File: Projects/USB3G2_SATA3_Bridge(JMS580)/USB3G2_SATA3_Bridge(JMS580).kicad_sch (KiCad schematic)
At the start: 74 parts, among them J1 ATA-A, J2 USB_C_Receptacle, Q1 Q_NPN_EBC, Q2 AO3401A, Q3 AO3400A, U1 W25Q32JVZP, U2 JMS580, U3 FP6381A, Y1 Crystal_GND24

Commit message: finish prj USB3G2_SATA3_Bridge(JMS580)
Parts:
- added H4: MountingHole, Symbol:ESD-Logo_6.6x6mm_SilkScreen, symbol Mechanical:MountingHole
- R1: footprint Resistor_SMD:R_0402_1005Metric -> Resistor_SMD:R_0603_1608Metric
- TP1, TP2: footprint (none) -> TestPoint:TestPoint_Pad_D1.0mm
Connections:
- no-connect marks 7 -> 9
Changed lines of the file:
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@@
   (no_connect (at 39.37 63.5))
   (no_connect (at 39.37 58.42))
+  (no_connect (at 133.35 115.57))
+  (no_connect (at 133.35 113.03))
   (no_connect (at 134.62 115.57))
   (no_connect (at 134.62 113.03))
@@
       (effects (font (size 1.27 1.27)) (justify left) hide)
     )
-    (property "Footprint" "" (id 2) (at 172.72 185.42 0)
+    (property "Footprint" "TestPoint:TestPoint_Pad_D1.0mm" (id 2) (at 172.72 185.42 0)
       (effects (font (size 1.27 1.27)) hide)
     )
@@
       (effects (font (size 1.27 1.27)) (justify left) hide)
     )
-    (property "Footprint" "" (id 2) (at 172.72 187.96 0)
+    (property "Footprint" "TestPoint:TestPoint_Pad_D1.0mm" (id 2) (at 172.72 187.96 0)
       (effects (font (size 1.27 1.27)) hide)
     )
@@
     )
   )
+  (symbol (lib_id "Mechanical:MountingHole") (at 44.45 213.36 0) (unit 1)
+    (in_bom yes) (on_board yes) (fields_autoplaced)
+    (property "Reference" "H4" (id 0) (at 46.99 212.4515 0)
+      (effects (font (size 1.27 1.27)) (justify left))
+    )
+    (property "Value" "MountingHole" (id 1) (at 46.99 215.2266 0)
+      (effects (font (size 1.27 1.27)) (justify left))
+    )
+    (property "Footprint" "Symbol:ESD-Logo_6.6x6mm_SilkScreen" (id 2) (at 44.45 213.36 0)
+      (effects (font (size 1.27 1.27)) hide)
+    )
+    (property "Datasheet" "~" (id 3) (at 44.45 213.36 0)
+      (effects (font (size 1.27 1.27)) hide)
+    )
+  )
   (symbol (lib_id "power:GND") (at 229.87 52.07 0) (unit 1)
     (in_bom yes) (on_board yes)
@@
     (property "Reference" "R1" (id 0) (at 251.46 154.94 90))
     (property "Value" "0R" (id 1) (at 251.46 152.4 90))
-    (property "Footprint" "Resistor_SMD:R_0402_1005Metric" (id 2) (at 251.46 153.162 90)
+    (property "Footprint" "Resistor_SMD:R_0603_1608Metric" (id 2) (at 251.46 153.162 90)
       (effects (font (size 1.27 1.27)) hide)
     )
@@
       (reference "H3") (unit 1) (value "MountingHole") (footprint "MountingHole:MountingHole_2.2mm_M2_Pad_Via")
     )
+    (path "/aa5e381f-9af5-4fa9-8bc8-1fe45b001137"
+      (reference "H4") (unit 1) (value "MountingHole") (footprint "Symbol:ESD-Logo_6.6x6mm_SilkScreen")
+    )
     (path "/b97d5994-9bcb-4763-85c8-744d5971f71d"
       (reference "J1") (unit 1) (value "ATA-A") (footprint "lib:SATA-22P-M")
@@
     )
     (path "/f19ab928-a71b-4fdd-893d-289cb4b88ac7"
-      (reference "R1") (unit 1) (value "0R") (footprint "Resistor_SMD:R_0402_1005Metric")
+      (reference "R1") (unit 1) (value "0R") (footprint "Resistor_SMD:R_0603_1608Metric")
     )
     (path "/25f163c8-b901-4e86-8aef-3e24ed3f1f2b"
@@
     )
     (path "/9324a5d8-df10-40f4-a586-be13060eaaaa"
-      (reference "TP1") (unit 1) (value "TestPoint") (footprint "")
+      (reference "TP1") (unit 1) (value "TestPoint") (footprint "TestPoint:TestPoint_Pad_D1.0mm")
     )
     (path "/96bcae62-54a4-4017-ba90-ec5c8ae58df7"
-      (reference "TP2") (unit 1) (value "TestPoint") (footprint "")
+      (reference "TP2") (unit 1) (value "TestPoint") (footprint "TestPoint:TestPoint_Pad_D1.0mm")
     )
     (path "/3f90ca07-e4d3-4f1b-91dd-571765506dae"

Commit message: add new prj
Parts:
- Q1: footprint Package_TO_SOT_SMD:TSOT-23 -> Package_TO_SOT_SMD:SOT-23
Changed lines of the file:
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@@
       (effects (font (size 1.27 1.27)) (justify left))
     )
-    (property "Footprint" "Package_TO_SOT_SMD:TSOT-23" (id 2) (at 251.46 119.38 0)
+    (property "Footprint" "Package_TO_SOT_SMD:SOT-23" (id 2) (at 251.46 119.38 0)
       (effects (font (size 1.27 1.27)) hide)
     )
@@
     )
     (path "/1edb2be0-b3e0-46f5-bfe4-e9c67541b25b"
-      (reference "Q1") (unit 1) (value "Q_NPN_EBC") (footprint "Package_TO_SOT_SMD:TSOT-23")
+      (reference "Q1") (unit 1) (value "Q_NPN_EBC") (footprint "Package_TO_SOT_SMD:SOT-23")
     )
     (path "/4d95e323-6704-4eb1-a19c-f033972fd2a0"

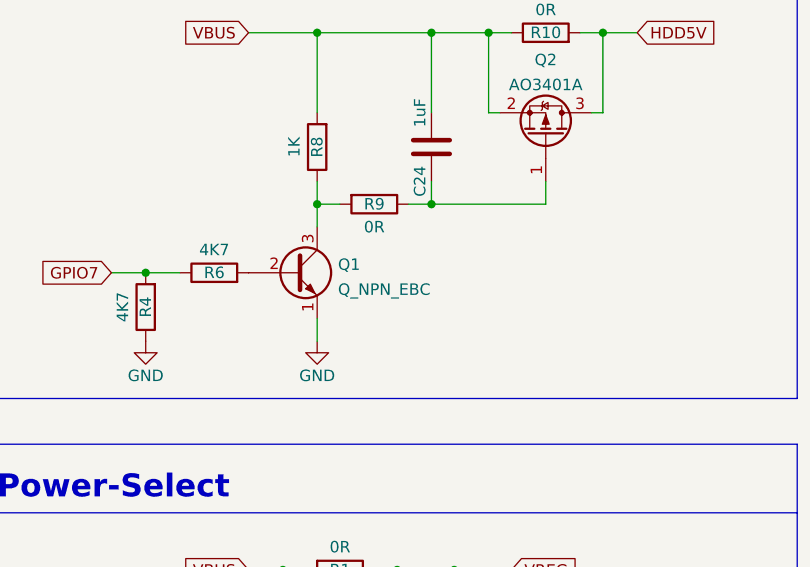
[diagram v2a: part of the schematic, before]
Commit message: Fix USB3G2_SATA3_Bridge(JMS580) 1AM Pinout
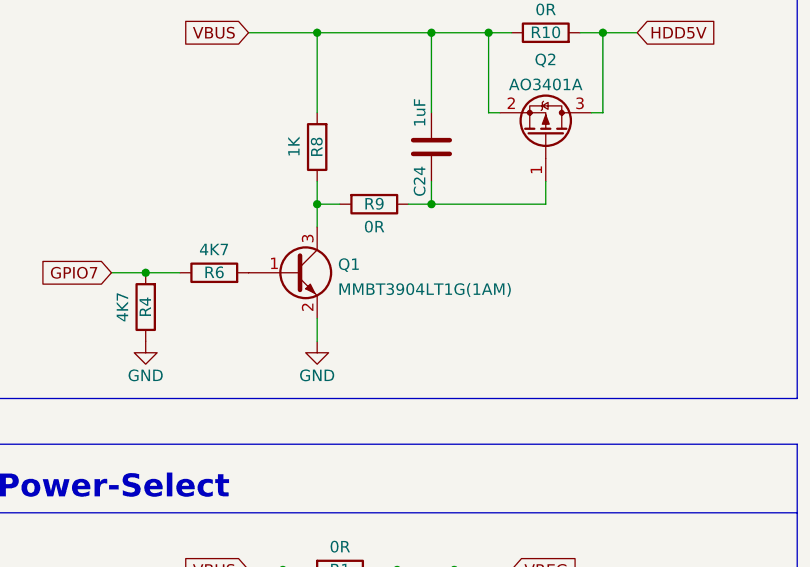
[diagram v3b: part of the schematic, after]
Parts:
- Q1: value Q_NPN_EBC -> MMBT3904LT1G(1AM); symbol Device:Q_NPN_EBC -> Device:Q_NPN_BEC
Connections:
- net GND: now also Q1.2 (E); no longer Q1.1 (E)
- net at R6.2: now also Q1.1 (B); no longer Q1.2 (B)
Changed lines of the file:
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@@
     (pin "2")
   )
-  (symbol (lib_id "Device:Q_NPN_EBC") (at 246.38 121.92 0) (unit 1)
+  (symbol (lib_id "Device:Q_NPN_BEC") (at 246.38 121.92 0) (unit 1)
     (in_bom yes) (on_board yes) (fields_autoplaced)
     (property "Reference" "Q1" (id 0) (at 251.2314 121.0115 0)
       (effects (font (size 1.27 1.27)) (justify left))
     )
-    (property "Value" "Q_NPN_EBC" (id 1) (at 251.2314 123.7866 0)
+    (property "Value" "MMBT3904LT1G(1AM)" (id 1) (at 251.2314 123.7866 0)
       (effects (font (size 1.27 1.27)) (justify left))
     )
@@
     )
     (path "/1edb2be0-b3e0-46f5-bfe4-e9c67541b25b"
-      (reference "Q1") (unit 1) (value "Q_NPN_EBC") (footprint "Package_TO_SOT_SMD:SOT-23")
+      (reference "Q1") (unit 1) (value "MMBT3904LT1G(1AM)") (footprint "Package_TO_SOT_SMD:SOT-23")
     )
     (path "/4d95e323-6704-4eb1-a19c-f033972fd2a0"

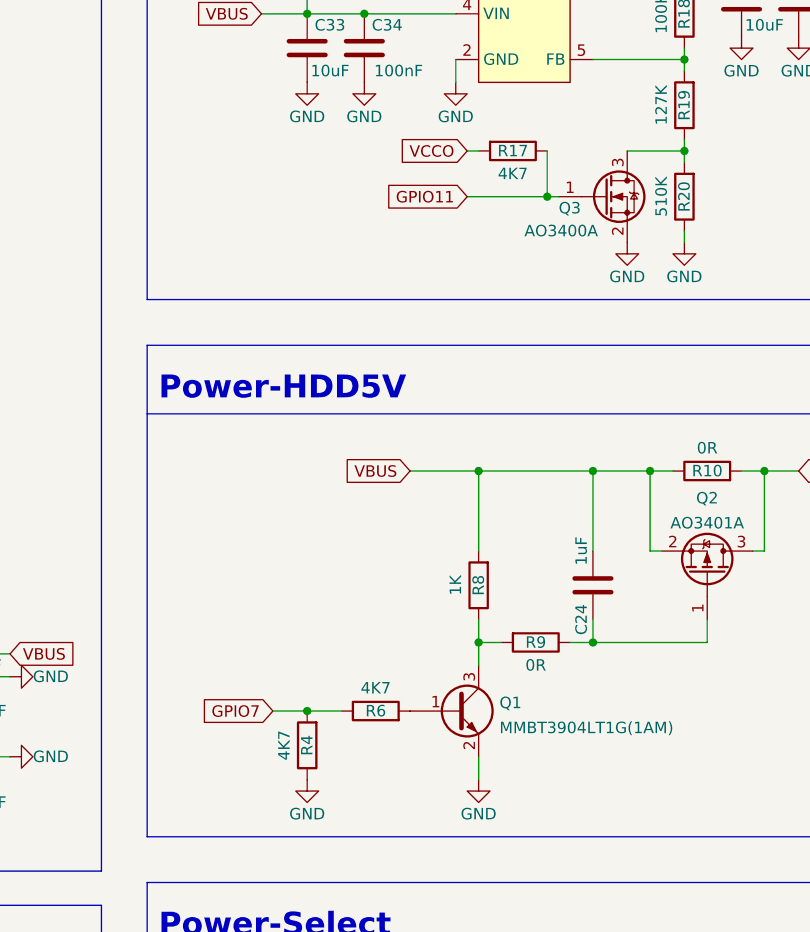
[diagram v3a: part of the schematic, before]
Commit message: Symbol Value unified
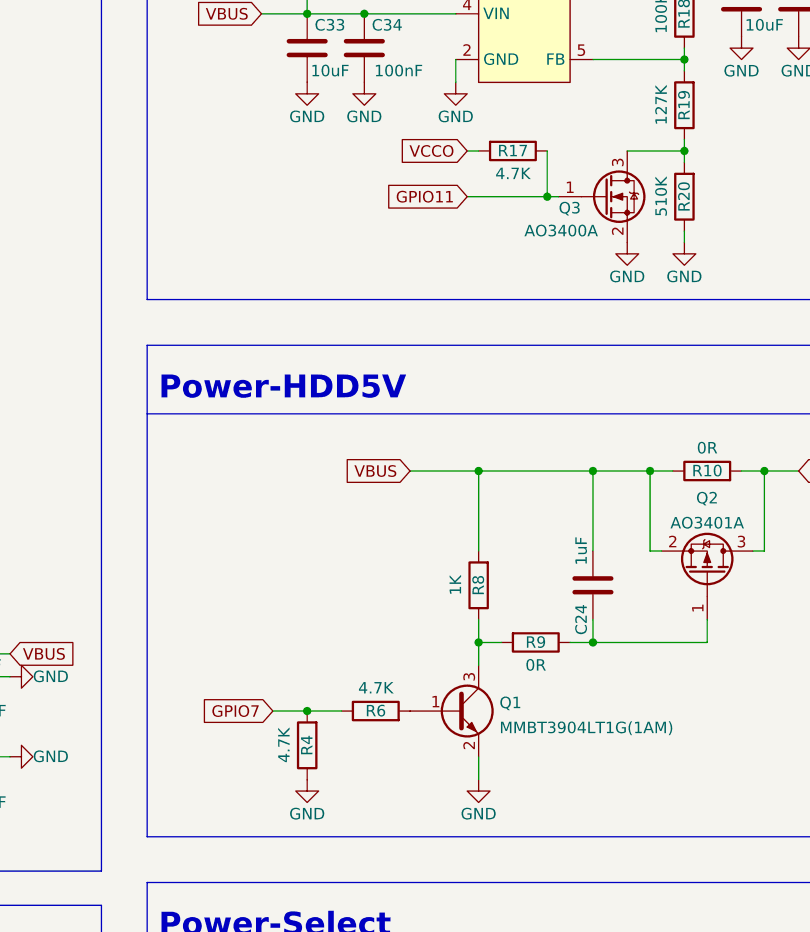
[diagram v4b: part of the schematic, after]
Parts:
- R17, R4, R6: value 4K7 -> 4.7K
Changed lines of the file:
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@@
     (in_bom yes) (on_board yes)
     (property "Reference" "R4" (id 0) (at 229.87 125.73 90))
-    (property "Value" "4K7" (id 1) (at 227.33 125.73 90))
+    (property "Value" "4.7K" (id 1) (at 227.33 125.73 90))
     (property "Footprint" "Resistor_SMD:R_0402_1005Metric" (id 2) (at 231.648 125.73 90)
       (effects (font (size 1.27 1.27)) hide)
@@
     (in_bom yes) (on_board yes)
     (property "Reference" "R6" (id 0) (at 237.49 121.92 90))
-    (property "Value" "4K7" (id 1) (at 237.49 119.38 90))
+    (property "Value" "4.7K" (id 1) (at 237.49 119.38 90))
     (property "Footprint" "Resistor_SMD:R_0402_1005Metric" (id 2) (at 237.49 123.698 90)
       (effects (font (size 1.27 1.27)) hide)
@@
     (in_bom yes) (on_board yes)
     (property "Reference" "R17" (id 0) (at 252.73 59.69 90))
-    (property "Value" "4K7" (id 1) (at 252.73 62.23 90))
+    (property "Value" "4.7K" (id 1) (at 252.73 62.23 90))
     (property "Footprint" "Resistor_SMD:R_0402_1005Metric" (id 2) (at 252.73 57.912 90)
       (effects (font (size 1.27 1.27)) hide)
@@
     )
     (path "/33310d76-3737-42f0-a38e-45b14928c7dd"
-      (reference "R4") (unit 1) (value "4K7") (footprint "Resistor_SMD:R_0402_1005Metric")
+      (reference "R4") (unit 1) (value "4.7K") (footprint "Resistor_SMD:R_0402_1005Metric")
     )
     (path "/20cd0897-de99-4398-b97c-f8d47b7f76a0"
@@
     )
     (path "/8f39036b-42db-4ec4-bdcd-4e6c2f0b0f66"
-      (reference "R6") (unit 1) (value "4K7") (footprint "Resistor_SMD:R_0402_1005Metric")
+      (reference "R6") (unit 1) (value "4.7K") (footprint "Resistor_SMD:R_0402_1005Metric")
     )
     (path "/b065e418-40da-4eb8-a0e4-34e07e6a886a"
@@
     )
     (path "/a1d9da60-23e2-4ea6-b26b-8ab9418510c3"
-      (reference "R17") (unit 1) (value "4K7") (footprint "Resistor_SMD:R_0402_1005Metric")
+      (reference "R17") (unit 1) (value "4.7K") (footprint "Resistor_SMD:R_0402_1005Metric")
     )
     (path "/5754544a-f0a2-46bf-90ae-96344532fafe"

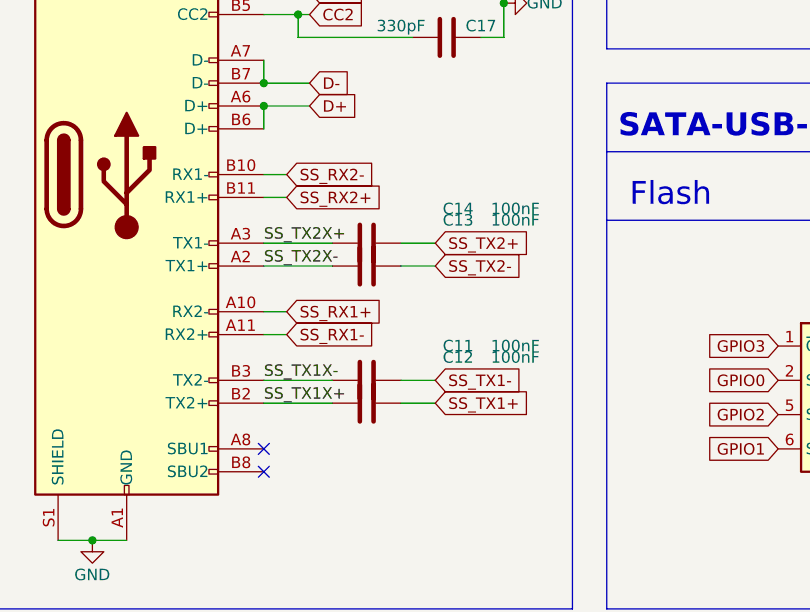
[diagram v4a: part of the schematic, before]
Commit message: USB3G2_SATA3_Bridge(JMS580) Error Fix (USB3.0 TX RX Swap problem)
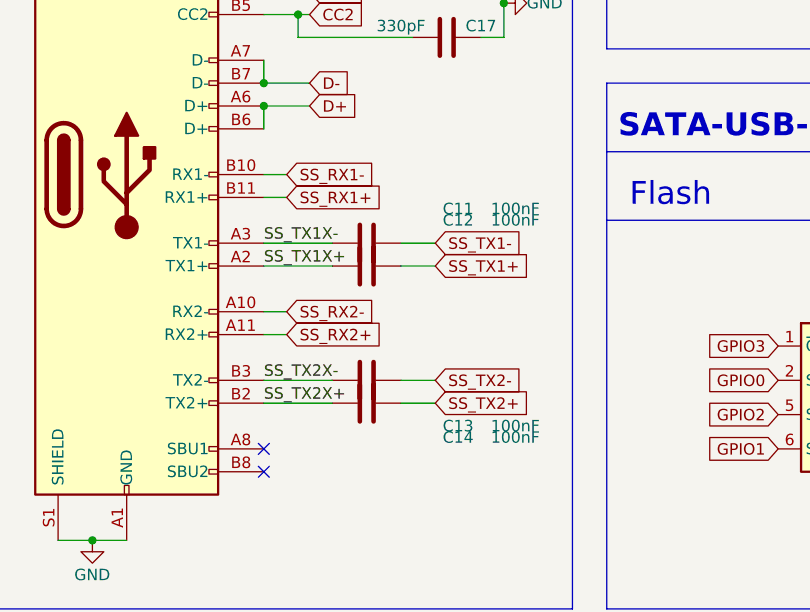
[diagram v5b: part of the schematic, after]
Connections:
- net SS_RX1+: now also J2.B11 (RX1+); no longer J2.A10 (RX2-)
- net SS_RX1-: now also J2.B10 (RX1-); no longer J2.A11 (RX2+)
- net SS_RX2+: now also J2.A11 (RX2+); no longer J2.B11 (RX1+)
- net SS_RX2-: now also J2.A10 (RX2-); no longer J2.B10 (RX1-)
- net SS_TX1X+: now also J2.A2 (TX1+); no longer J2.B2 (TX2+)
- net SS_TX1X-: now also J2.A3 (TX1-); no longer J2.B3 (TX2-)
- net SS_TX2X+: now also J2.B2 (TX2+); no longer J2.A3 (TX1-)
- net SS_TX2X-: now also J2.B3 (TX2-); no longer J2.A2 (TX1+)
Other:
- moved on the sheet: C11, C12, C13, C14

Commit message: Fix layout
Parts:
- R10: value 0R -> 0R / NS
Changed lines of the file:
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@@
     (in_bom yes) (on_board yes)
     (property "Reference" "R10" (id 0) (at 274.32 95.25 90))
-    (property "Value" "0R" (id 1) (at 274.32 92.71 90))
+    (property "Value" "0R / NS" (id 1) (at 274.32 92.71 90))
     (property "Footprint" "Resistor_SMD:R_0402_1005Metric" (id 2) (at 274.32 97.028 90)
       (effects (font (size 1.27 1.27)) hide)
@@
     )
     (path "/64fe547e-6259-4a54-9b77-8018a1c05709"
-      (reference "R10") (unit 1) (value "0R") (footprint "Resistor_SMD:R_0402_1005Metric")
+      (reference "R10") (unit 1) (value "0R / NS") (footprint "Resistor_SMD:R_0402_1005Metric")
     )
     (path "/a6ed30d5-b3a0-4409-81c2-f6b3b8353609"

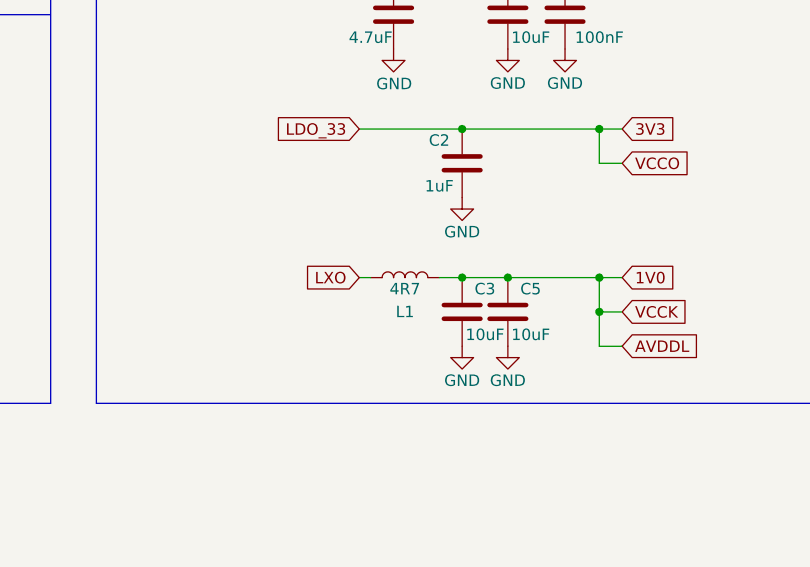
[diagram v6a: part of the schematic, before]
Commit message: Update description in Sch
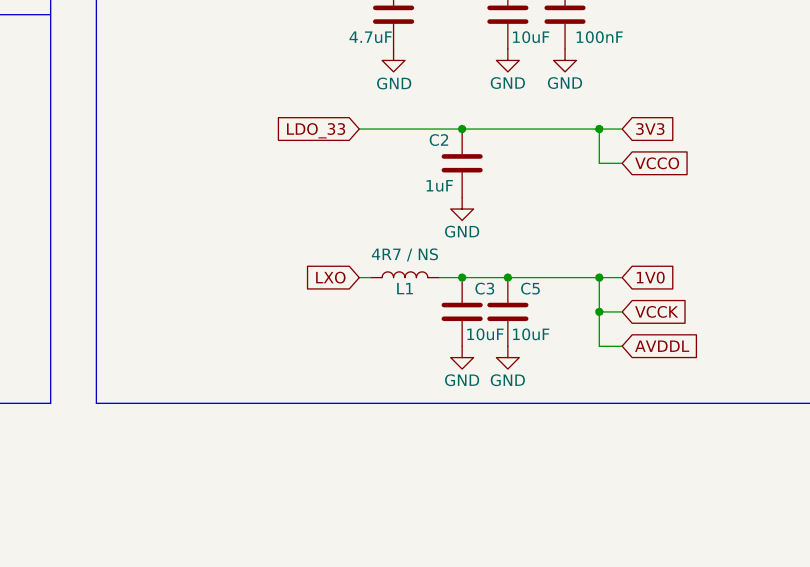
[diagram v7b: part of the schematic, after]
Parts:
- L1: value 4R7 -> 4R7 / NS
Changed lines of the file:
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@@
   (symbol (lib_id "Device:L") (at 246.38 187.96 270) (mirror x) (unit 1)
     (in_bom yes) (on_board yes)
-    (property "Reference" "L1" (id 0) (at 246.38 191.77 90))
-    (property "Value" "4R7" (id 1) (at 246.38 189.23 90))
+    (property "Reference" "L1" (id 0) (at 246.38 189.23 90))
+    (property "Value" "4R7 / NS" (id 1) (at 246.38 185.42 90))
     (property "Footprint" "Inductor_SMD:L_Neosid_SMS-ME3015" (id 2) (at 246.38 187.96 0)
       (effects (font (size 1.27 1.27)) hide)
@@
     )
     (path "/85e25dad-19a5-422e-a3d1-8d0de62da00e"
-      (reference "L1") (unit 1) (value "4R7") (footprint "Inductor_SMD:L_Neosid_SMS-ME3015")
+      (reference "L1") (unit 1) (value "4R7 / NS") (footprint "Inductor_SMD:L_Neosid_SMS-ME3015")
     )
     (path "/ba050d1b-23c3-4300-94f4-d2d79b7ef8d1"

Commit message: Sort Out
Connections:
- no-connect marks 9 -> 8
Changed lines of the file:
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@@
   (junction (at 241.3 39.37) (diameter 0) (color 0 0 0 0)
   )
-  (no_connect (at 49.53 184.15))
   (no_connect (at 49.53 186.69))
   (no_connect (at 39.37 60.96))
@@
     (pin "A6")
     (pin "A7")
-    (pin "A8")
     (pin "A9")
     (pin "B1")
